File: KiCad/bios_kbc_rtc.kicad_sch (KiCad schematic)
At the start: 33 parts, among them J1 PS/2 Dual Port, U1 8242KBD, U10 BANK0, U11 BANK0, U12 BANK1, U13 BANK1, U2 74HC05, U3 SST39SF010A, U4 DS12885, X1 32768Hz

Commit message: Version 1.4: Move mounting holes to ATX compatible locations
Signed-off-by: Sergey Kiselev <skiselev@gmail.com>
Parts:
- removed R27: 150, My_Components:Res_Axial_L6.3mm_D2.5mm_P10.16mm_Horizontal, symbol Device:R
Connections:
- net PW_LED_PLUS: now reaches JP3.1 (Pin_1)
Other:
- moved on the sheet: JP3
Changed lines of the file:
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@@
   (junction (at 309.88 93.98) (diameter 0) (color 0 0 0 0)
   )
-  (junction (at 304.8 43.18) (diameter 0) (color 0 0 0 0)
+  (junction (at 307.34 43.18) (diameter 0) (color 0 0 0 0)
   )
   (junction (at 254 213.36) (diameter 0) (color 0 0 0 0)
@@
   (no_connect (at 152.4 208.28))
   (no_connect (at 71.12 231.14))
-  (no_connect (at 307.34 35.56))
+  (no_connect (at 309.88 35.56))
   (no_connect (at 254 50.8))
   (no_connect (at 254 68.58))
@@
     (stroke (width 0) (type default) (color 0 0 0 0))
   )
-  (wire (pts (xy 276.86 40.64) (xy 307.34 40.64))
-    (stroke (width 0) (type default) (color 0 0 0 0))
-  )
-  (wire (pts (xy 304.8 38.1) (xy 304.8 43.18))
+  (wire (pts (xy 276.86 40.64) (xy 309.88 40.64))
+    (stroke (width 0) (type default) (color 0 0 0 0))
+  )
+  (wire (pts (xy 307.34 38.1) (xy 307.34 43.18))
     (stroke (width 0) (type default) (color 0 0 0 0))
   )
@@
     (stroke (width 0) (type default) (color 0 0 0 0))
   )
-  (wire (pts (xy 294.64 33.02) (xy 292.1 33.02))
-    (stroke (width 0) (type default) (color 0 0 0 0))
-  )
   (wire (pts (xy 370.84 170.18) (xy 370.84 172.72))
     (stroke (width 0) (type default) (color 0 0 0 0))
@@
     (stroke (width 0) (type default) (color 0 0 0 0))
   )
-  (wire (pts (xy 302.26 33.02) (xy 307.34 33.02))
-    (stroke (width 0) (type default) (color 0 0 0 0))
-  )
-  (wire (pts (xy 292.1 30.48) (xy 292.1 33.02))
+  (wire (pts (xy 304.8 33.02) (xy 309.88 33.02))
     (stroke (width 0) (type default) (color 0 0 0 0))
   )
@@
     (stroke (width 0) (type default) (color 0 0 0 0))
   )
-  (wire (pts (xy 307.34 38.1) (xy 304.8 38.1))
+  (wire (pts (xy 309.88 38.1) (xy 307.34 38.1))
     (stroke (width 0) (type default) (color 0 0 0 0))
   )
@@
     (stroke (width 0) (type default) (color 0 0 0 0))
   )
-  (wire (pts (xy 304.8 43.18) (xy 304.8 45.72))
+  (wire (pts (xy 307.34 43.18) (xy 307.34 45.72))
     (stroke (width 0) (type default) (color 0 0 0 0))
   )
@@
     (stroke (width 0) (type default) (color 0 0 0 0))
   )
-  (wire (pts (xy 304.8 43.18) (xy 307.34 43.18))
+  (wire (pts (xy 307.34 43.18) (xy 309.88 43.18))
     (stroke (width 0) (type default) (color 0 0 0 0))
   )
@@
     (effects (font (size 1.27 1.27)) (justify right))
     (property "Intersheet References" "${INTERSHEET_REFS}" (id 0) (at 24.5593 208.2006 0)
+      (effects (font (size 1.27 1.27)) (justify right) hide)
+    )
+  )
+  (global_label "PW_LED_PLUS" (shape output) (at 304.8 33.02 180) (fields_autoplaced)
+    (effects (font (size 1.27 1.27)) (justify right))
+    (property "Intersheet References" "${INTERSHEET_REFS}" (id 0) (at 289.445 32.9406 0)
       (effects (font (size 1.27 1.27)) (justify right) hide)
     )
@@
     (pin "1")
   )
-  (symbol (lib_id "power:GND") (at 304.8 45.72 0) (unit 1)
-    (in_bom yes) (on_board yes)
-    (property "Reference" "#PWR0145" (id 0) (at 304.8 52.07 0)
-      (effects (font (size 1.27 1.27)) hide)
-    )
-    (property "Value" "GND" (id 1) (at 304.8 49.53 0))
-    (property "Footprint" "" (id 2) (at 304.8 45.72 0)
-      (effects (font (size 1.27 1.27)) hide)
-    )
-    (property "Datasheet" "" (id 3) (at 304.8 45.72 0)
+  (symbol (lib_id "power:GND") (at 307.34 45.72 0) (unit 1)
+    (in_bom yes) (on_board yes)
+    (property "Reference" "#PWR0145" (id 0) (at 307.34 52.07 0)
+      (effects (font (size 1.27 1.27)) hide)
+    )
+    (property "Value" "GND" (id 1) (at 307.34 49.53 0))
+    (property "Footprint" "" (id 2) (at 307.34 45.72 0)
+      (effects (font (size 1.27 1.27)) hide)
+    )
+    (property "Datasheet" "" (id 3) (at 307.34 45.72 0)
       (effects (font (size 1.27 1.27)) hide)
     )
@@
     (pin "11")
   )
-  (symbol (lib_id "power:VCC") (at 292.1 30.48 0) (unit 1)
-    (in_bom yes) (on_board yes)
-    (property "Reference" "#PWR0156" (id 0) (at 292.1 34.29 0)
-      (effects (font (size 1.27 1.27)) hide)
-    )
-    (property "Value" "VCC" (id 1) (at 292.1 26.67 0))
-    (property "Footprint" "" (id 2) (at 292.1 30.48 0)
-      (effects (font (size 1.27 1.27)) hide)
-    )
-    (property "Datasheet" "" (id 3) (at 292.1 30.48 0)
-      (effects (font (size 1.27 1.27)) hide)
-    )
-    (pin "1")
-  )
   (symbol (lib_id "Device:Crystal_GND3") (at 93.98 64.77 90) (unit 1)
     (in_bom yes) (on_board yes)
@@
     (pin "3")
   )
-  (symbol (lib_id "Connector_Generic:Conn_01x05") (at 312.42 38.1 0) (unit 1)
+  (symbol (lib_id "Connector_Generic:Conn_01x05") (at 314.96 38.1 0) (unit 1)
     (in_bom yes) (on_board yes) (fields_autoplaced)
-    (property "Reference" "JP3" (id 0) (at 314.96 36.8299 0)
+    (property "Reference" "JP3" (id 0) (at 317.5 36.8299 0)
       (effects (font (size 1.27 1.27)) (justify left))
     )
-    (property "Value" "POW LED / KEY LOCK" (id 1) (at 314.96 39.3699 0)
+    (property "Value" "POW LED / KEY LOCK" (id 1) (at 317.5 39.3699 0)
       (effects (font (size 1.27 1.27)) (justify left))
     )
-    (property "Footprint" "My_Components:Conn_Pin_Header_5x1_2.54mm" (id 2) (at 312.42 38.1 0)
-      (effects (font (size 1.27 1.27)) hide)
-    )
-    (property "Datasheet" "~" (id 3) (at 312.42 38.1 0)
+    (property "Footprint" "My_Components:Conn_Pin_Header_5x1_2.54mm" (id 2) (at 314.96 38.1 0)
+      (effects (font (size 1.27 1.27)) hide)
+    )
+    (property "Datasheet" "~" (id 3) (at 314.96 38.1 0)
       (effects (font (size 1.27 1.27)) hide)
     )
@@
     (pin "1")
   )
-  (symbol (lib_id "Device:R") (at 298.45 33.02 90) (unit 1)
-    (in_bom yes) (on_board yes)
-    (property "Reference" "R27" (id 0) (at 298.45 27.94 90))
-    (property "Value" "150" (id 1) (at 298.45 30.48 90))
-    (property "Footprint" "My_Components:Res_Axial_L6.3mm_D2.5mm_P10.16mm_Horizontal" (id 2) (at 298.45 34.798 90)
-      (effects (font (size 1.27 1.27)) hide)
-    )
-    (property "Datasheet" "~" (id 3) (at 298.45 33.02 0)
-      (effects (font (size 1.27 1.27)) hide)
-    )
-    (pin "1")
-    (pin "2")
-  )
   (symbol (lib_id "power:GND") (at 233.68 231.14 0) (unit 1)

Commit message: Version 1.6: Use half-can oscillators and low-profile crystal
Signed-off-by: Sergey Kiselev <skiselev@gmail.com>
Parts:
- removed RP4, RP5, RP6: 10, My_Components:Conn_SIL8, symbol Device:R_Pack04_SIP
- removed RP7: 100, My_Components:Conn_SIL8, symbol Device:R_Pack04_SIP
- added R38, R39, R40, R41, R42, R43, R44, R45, R46, R47, R48, R49: 10, My_Components:Res_762, symbol Device:R
- added R50, R51, R52, R53: 100, My_Components:Res_762, symbol Device:R
- R17, R18: footprint My_Components:Res_Axial_L6.3mm_D2.5mm_P10.16mm_Horizontal -> My_Components:Res_762
- renumbered X1 to Y2
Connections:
- net MA0: now also R39.1
- net MA1: now also R40.1
- net MA10: now also R45.1
- net MA2: now also R41.1
- net MA3: now also R46.1
- net MA4: now also R47.1
- net MA5: now also R48.1
- net MA6: now also R49.1
- net MA7: now also R42.1
- net MA8: now also R43.1
- net MA9: now also R44.1
- net RA0: now also R39.2
- net RA1: now also R40.2
- net RA10: now also R45.2
- net RA2: now also R41.2
- net RA3: now also R46.2
- net RA4: now also R47.2
- net RA5: now also R48.2
- net RA6: now also R49.2
- net RA7: now also R42.2
- net RA8: now also R43.2
- net RA9: now also R44.2
- net ~{MCAS0}: now also R50.1
- net ~{MCAS1}: now also R51.1
- net ~{MCAS2}: now also R52.1
- net ~{MCAS3}: now also R53.1
- net ~{MWE}: now also R38.1
- net ~{RCAS0}: now also R50.2
- net ~{RCAS1}: now also R51.2
- net ~{RCAS2}: now also R52.2
- net ~{RCAS3}: now also R53.2
- net ~{RWE}: now also R38.2

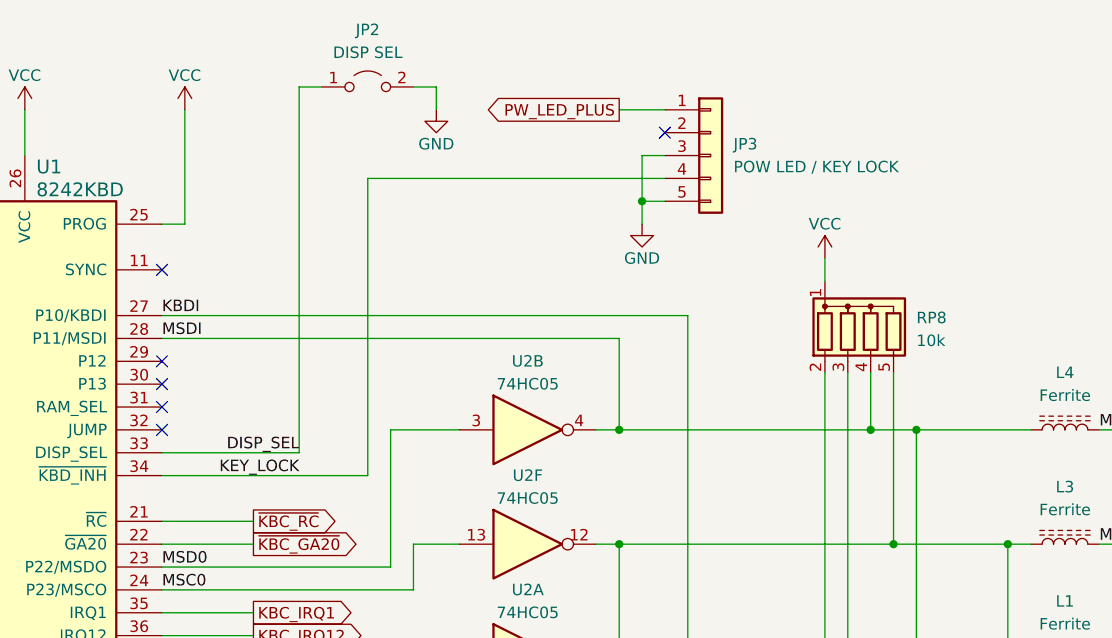
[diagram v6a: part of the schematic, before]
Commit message: Version 1.7: Use single front panel connector
Signed-off-by: Sergey Kiselev <skiselev@gmail.com>
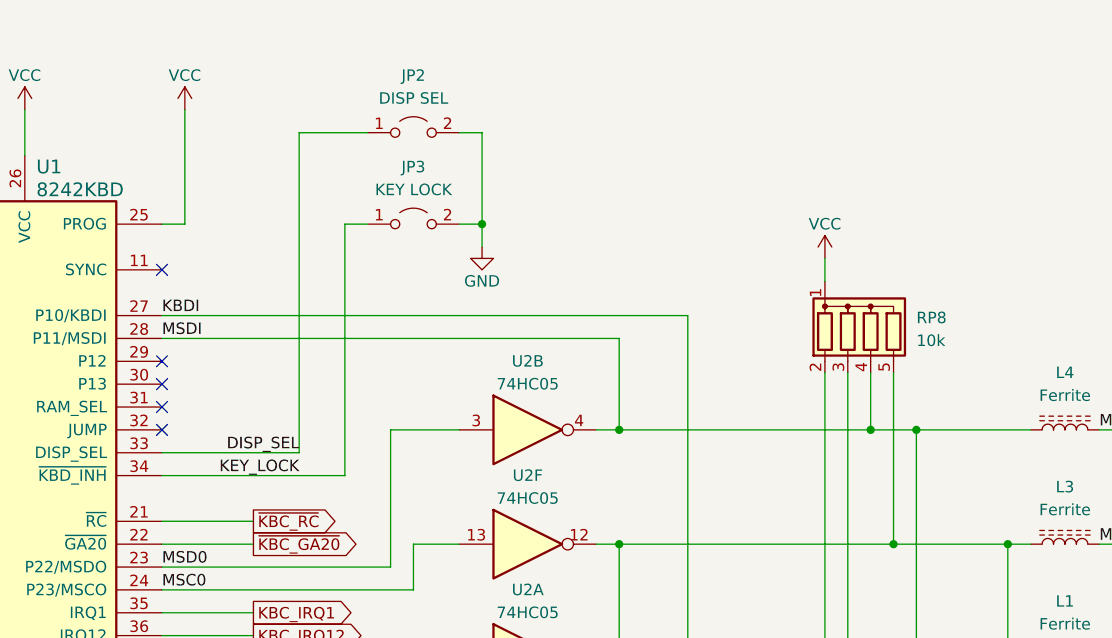
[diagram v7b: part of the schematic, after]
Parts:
- removed JP3: POW LED / KEY LOCK, My_Components:Conn_Pin_Header_5x1_2.54mm, symbol Connector_Generic:Conn_01x05
- added JP3: KEY LOCK, My_Components:Conn_Pin_Header_2x1_2.54mm, symbol Jumper:Jumper_2_Open
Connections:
- net GND: now also JP3.2 (B)
- net KEY_LOCK: now also JP3.1 (A)
- no-connect marks 14 -> 13
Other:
- moved on the sheet: JP2
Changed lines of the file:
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@@
   (junction (at 309.88 93.98) (diameter 0) (color 0 0 0 0)
   )
-  (junction (at 307.34 43.18) (diameter 0) (color 0 0 0 0)
-  )
   (junction (at 254 213.36) (diameter 0) (color 0 0 0 0)
   )
@@
   (junction (at 386.08 213.36) (diameter 0) (color 0 0 0 0)
   )
+  (junction (at 289.56 45.72) (diameter 0) (color 0 0 0 0)
+  )
   (junction (at 335.28 81.28) (diameter 0) (color 0 0 0 0)
   )
@@
   (no_connect (at 152.4 208.28))
   (no_connect (at 71.12 231.14))
-  (no_connect (at 309.88 35.56))
   (no_connect (at 254 50.8))
   (no_connect (at 254 68.58))
@@
     (stroke (width 0) (type default) (color 0 0 0 0))
   )
-  (wire (pts (xy 276.86 40.64) (xy 309.88 40.64))
-    (stroke (width 0) (type default) (color 0 0 0 0))
-  )
-  (wire (pts (xy 307.34 38.1) (xy 307.34 43.18))
-    (stroke (width 0) (type default) (color 0 0 0 0))
-  )
   (wire (pts (xy 226.06 246.38) (xy 231.14 246.38))
     (stroke (width 0) (type default) (color 0 0 0 0))
@@
     (stroke (width 0) (type default) (color 0 0 0 0))
   )
+  (wire (pts (xy 289.56 45.72) (xy 289.56 48.26))
+    (stroke (width 0) (type default) (color 0 0 0 0))
+  )
   (wire (pts (xy 302.26 170.18) (xy 302.26 172.72))
     (stroke (width 0) (type default) (color 0 0 0 0))
@@
     (stroke (width 0) (type default) (color 0 0 0 0))
   )
-  (wire (pts (xy 269.24 30.48) (xy 269.24 71.12))
+  (wire (pts (xy 269.24 35.56) (xy 269.24 71.12))
     (stroke (width 0) (type default) (color 0 0 0 0))
   )
@@
     (stroke (width 0) (type default) (color 0 0 0 0))
   )
-  (wire (pts (xy 254 73.66) (xy 276.86 73.66))
+  (wire (pts (xy 254 73.66) (xy 274.32 73.66))
     (stroke (width 0) (type default) (color 0 0 0 0))
   )
@@
     (stroke (width 0) (type default) (color 0 0 0 0))
   )
-  (wire (pts (xy 271.78 30.48) (xy 269.24 30.48))
+  (wire (pts (xy 276.86 35.56) (xy 269.24 35.56))
     (stroke (width 0) (type default) (color 0 0 0 0))
   )
@@
     (stroke (width 0) (type default) (color 0 0 0 0))
   )
+  (wire (pts (xy 274.32 45.72) (xy 276.86 45.72))
+    (stroke (width 0) (type default) (color 0 0 0 0))
+  )
   (wire (pts (xy 182.88 215.9) (xy 185.42 215.9))
     (stroke (width 0) (type default) (color 0 0 0 0))
@@
     (stroke (width 0) (type default) (color 0 0 0 0))
   )
-  (wire (pts (xy 281.94 30.48) (xy 284.48 30.48))
+  (wire (pts (xy 287.02 35.56) (xy 289.56 35.56))
     (stroke (width 0) (type default) (color 0 0 0 0))
   )
@@
     (stroke (width 0) (type default) (color 0 0 0 0))
   )
-  (wire (pts (xy 304.8 33.02) (xy 309.88 33.02))
-    (stroke (width 0) (type default) (color 0 0 0 0))
-  )
   (wire (pts (xy 269.24 71.12) (xy 254 71.12))
     (stroke (width 0) (type default) (color 0 0 0 0))
@@
     (stroke (width 0) (type default) (color 0 0 0 0))
   )
+  (wire (pts (xy 287.02 45.72) (xy 289.56 45.72))
+    (stroke (width 0) (type default) (color 0 0 0 0))
+  )
   (wire (pts (xy 208.28 101.6) (xy 213.36 101.6))
     (stroke (width 0) (type default) (color 0 0 0 0))
@@
     (stroke (width 0) (type default) (color 0 0 0 0))
   )
-  (wire (pts (xy 309.88 38.1) (xy 307.34 38.1))
-    (stroke (width 0) (type default) (color 0 0 0 0))
-  )
   (wire (pts (xy 304.8 81.28) (xy 335.28 81.28))
     (stroke (width 0) (type default) (color 0 0 0 0))
@@
     (stroke (width 0) (type default) (color 0 0 0 0))
   )
-  (wire (pts (xy 307.34 43.18) (xy 307.34 45.72))
-    (stroke (width 0) (type default) (color 0 0 0 0))
-  )
   (wire (pts (xy 81.28 101.6) (xy 86.36 101.6))
     (stroke (width 0) (type default) (color 0 0 0 0))
@@
     (stroke (width 0) (type default) (color 0 0 0 0))
   )
-  (wire (pts (xy 307.34 43.18) (xy 309.88 43.18))
-    (stroke (width 0) (type default) (color 0 0 0 0))
-  )
   (wire (pts (xy 109.22 269.24) (xy 114.3 269.24))
     (stroke (width 0) (type default) (color 0 0 0 0))
@@
     (stroke (width 0) (type default) (color 0 0 0 0))
   )
-  (wire (pts (xy 276.86 73.66) (xy 276.86 40.64))
+  (wire (pts (xy 274.32 73.66) (xy 274.32 45.72))
     (stroke (width 0) (type default) (color 0 0 0 0))
   )
@@
     (stroke (width 0) (type default) (color 0 0 0 0))
   )
-  (wire (pts (xy 284.48 30.48) (xy 284.48 33.02))
+  (wire (pts (xy 289.56 35.56) (xy 289.56 45.72))
     (stroke (width 0) (type default) (color 0 0 0 0))
   )
@@
     )
   )
-  (global_label "PW_LED_PLUS" (shape output) (at 304.8 33.02 180) (fields_autoplaced)
-    (effects (font (size 1.27 1.27)) (justify right))
-    (property "Intersheet References" "${INTERSHEET_REFS}" (id 0) (at 289.445 32.9406 0)
-      (effects (font (size 1.27 1.27)) (justify right) hide)
-    )
-  )
   (global_label "D7" (shape tri_state) (at 264.16 198.12 0) (fields_autoplaced)
     (effects (font (size 1.27 1.27)) (justify left))
@@
     (pin "1")
   )
-  (symbol (lib_id "power:GND") (at 307.34 45.72 0) (unit 1)
-    (in_bom yes) (on_board yes)
-    (property "Reference" "#PWR0145" (id 0) (at 307.34 52.07 0)
-      (effects (font (size 1.27 1.27)) hide)
-    )
-    (property "Value" "GND" (id 1) (at 307.34 49.53 0))
-    (property "Footprint" "" (id 2) (at 307.34 45.72 0)
-      (effects (font (size 1.27 1.27)) hide)
-    )
-    (property "Datasheet" "" (id 3) (at 307.34 45.72 0)
-      (effects (font (size 1.27 1.27)) hide)
-    )
-    (pin "1")
-  )
   (symbol (lib_id "power:VCC") (at 170.18 170.18 0) (unit 1)
     (in_bom yes) (on_board yes)
@@
     (pin "2")
   )
-  (symbol (lib_id "Connector_Generic:Conn_01x05") (at 314.96 38.1 0) (unit 1)
-    (in_bom yes) (on_board yes) (fields_autoplaced)
-    (property "Reference" "JP3" (id 0) (at 317.5 36.8299 0)
-      (effects (font (size 1.27 1.27)) (justify left))
-    )
-    (property "Value" "POW LED / KEY LOCK" (id 1) (at 317.5 39.3699 0)
-      (effects (font (size 1.27 1.27)) (justify left))
-    )
-    (property "Footprint" "My_Components:Conn_Pin_Header_5x1_2.54mm" (id 2) (at 314.96 38.1 0)
-      (effects (font (size 1.27 1.27)) hide)
-    )
-    (property "Datasheet" "~" (id 3) (at 314.96 38.1 0)
-      (effects (font (size 1.27 1.27)) hide)
-    )
-    (pin "1")
-    (pin "2")
-    (pin "3")
-    (pin "4")
-    (pin "5")
-  )
   (symbol (lib_id "power:GND") (at 337.82 119.38 0) (unit 1)
     (in_bom yes) (on_board yes)
@@
     (pin "2")
   )
+  (symbol (lib_id "Jumper:Jumper_2_Open") (at 281.94 45.72 0) (unit 1)
+    (in_bom yes) (on_board yes) (fields_autoplaced)
+    (property "Reference" "JP3" (id 0) (at 281.94 39.37 0))
+    (property "Value" "KEY LOCK" (id 1) (at 281.94 41.91 0))
+    (property "Footprint" "My_Components:Conn_Pin_Header_2x1_2.54mm" (id 2) (at 281.94 45.72 0)
+      (effects (font (size 1.27 1.27)) hide)
+    )
+    (property "Datasheet" "~" (id 3) (at 281.94 45.72 0)
+      (effects (font (size 1.27 1.27)) hide)
+    )
+    (pin "1")
+    (pin "2")
+  )
   (symbol (lib_id "power:VCC") (at 238.76 33.02 0) (unit 1)
     (in_bom yes) (on_board yes)
@@
     (pin "1")
   )
+  (symbol (lib_id "power:GND") (at 289.56 48.26 0) (unit 1)
+    (in_bom yes) (on_board yes)
+    (property "Reference" "#PWR0146" (id 0) (at 289.56 54.61 0)
+      (effects (font (size 1.27 1.27)) hide)
+    )
+    (property "Value" "GND" (id 1) (at 289.56 52.07 0))
+    (property "Footprint" "" (id 2) (at 289.56 48.26 0)
+      (effects (font (size 1.27 1.27)) hide)
+    )
+    (property "Datasheet" "" (id 3) (at 289.56 48.26 0)
+      (effects (font (size 1.27 1.27)) hide)
+    )
+    (pin "1")
+  )
   (symbol (lib_id "Device:R") (at 157.48 246.38 90) (unit 1)
     (in_bom yes) (on_board yes)
@@
     (pin "1")
   )
-  (symbol (lib_id "Jumper:Jumper_2_Open") (at 276.86 30.48 0) (unit 1)
+  (symbol (lib_id "Jumper:Jumper_2_Open") (at 281.94 35.56 0) (unit 1)
     (in_bom yes) (on_board yes) (fields_autoplaced)
-    (property "Reference" "JP2" (id 0) (at 276.86 24.13 0))
-    (property "Value" "DISP SEL" (id 1) (at 276.86 26.67 0))
-    (property "Footprint" "My_Components:Conn_Pin_Header_2x1_2.54mm" (id 2) (at 276.86 30.48 0)
+    (property "Reference" "JP2" (id 0) (at 281.94 29.21 0))
+    (property "Value" "DISP SEL" (id 1) (at 281.94 31.75 0))
+    (property "Footprint" "My_Components:Conn_Pin_Header_2x1_2.54mm" (id 2) (at 281.94 35.56 0)
       (effects (font (size 1.27 1.27)) hide)
     )
-    (property "Datasheet" "~" (id 3) (at 276.86 30.48 0)
+    (property "Datasheet" "~" (id 3) (at 281.94 35.56 0)
       (effects (font (size 1.27 1.27)) hide)
     )
@@
       (effects (font (size 1.27 1.27)) hide)
     )
-    (pin "1")
-  )
-  (symbol (lib_id "power:GND") (at 284.48 33.02 0) (unit 1)
-    (in_bom yes) (on_board yes)
-    (property "Reference" "#PWR0215" (id 0) (at 284.48 39.37 0)
-      (effects (font (size 1.27 1.27)) hide)
-    )
-    (property "Value" "GND" (id 1) (at 284.48 36.83 0))
-    (property "Footprint" "" (id 2) (at 284.48 33.02 0)
-      (effects (font (size 1.27 1.27)) hide)
-    )
-    (property "Datasheet" "" (id 3) (at 284.48 33.02 0)
-      (effects (font (size 1.27 1.27)) hide)
-    )
